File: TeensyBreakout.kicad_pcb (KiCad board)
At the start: 2 copper layers, 149 parts, among them CON1 SJ-3523-SMT-TR, CON2 Headphone, CON3 Line In, IC1 ZLDO1117G33, IC2 NCP1117ST50T3G, J1 73725-0110BLF, J2 Conn_01x02, J3 RJ45_LED, J4 PJ-102A, J5 SPKLEFT, J6 SPKRIGHT, J7 PJ-102A, J8 Conn_01x14, Q1 FDN340P, Q1A1 BSD223P, Q1B1 BSD223P, Q2 BSS138, Q3 AOD417, Q4 BSS138, Q5 BSS138, SW1 SW_MEC_5E, U1 Teensy4.1, U2 ESP-WROOM-02, U3 MAX9744ETH_T, U4 MIC5225-3.3, U5 SGTL5000XNAA3, X1 332-06, X2 Conn_01x05, X3 Conn_01x03

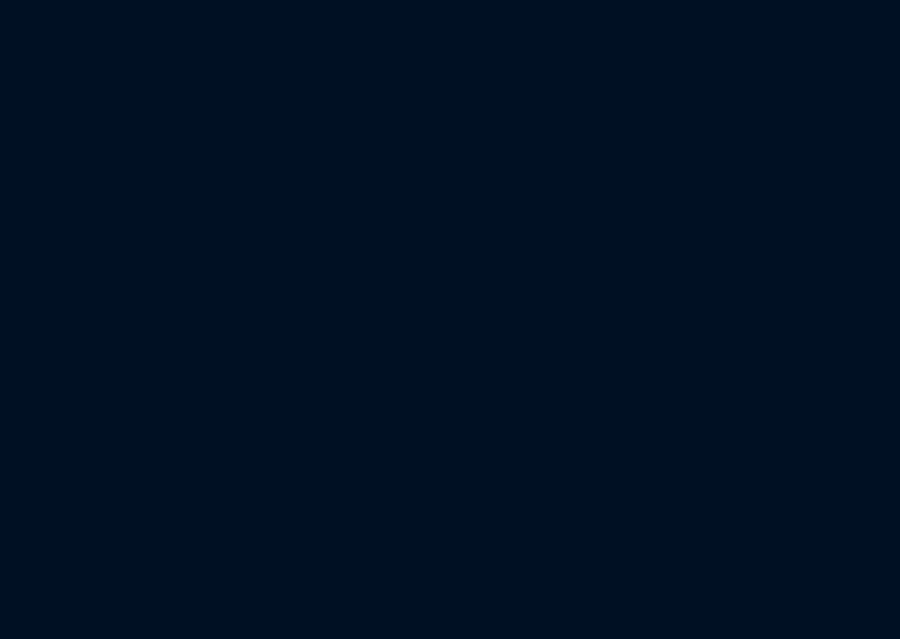
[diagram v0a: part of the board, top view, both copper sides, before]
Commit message: removing old amp, can't buy chip
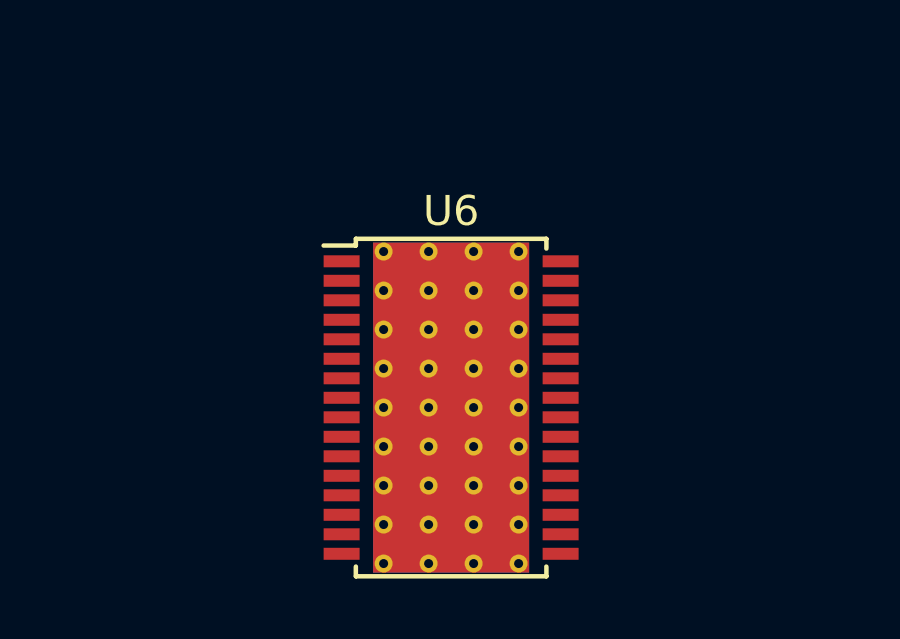
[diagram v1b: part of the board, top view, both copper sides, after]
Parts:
- added U6: TPA3126D2, Package_SO:HTSSOP-32-1EP_6.1x11mm_P0.65mm_EP5.2x11mm_Mask4.11x4.36mm_ThermalVias, F.Cu at (81.6, 121.4)

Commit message: making layout
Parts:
- removed C10, C11, C16, C17: 470pF, Capacitor_SMD:C_0603_1608Metric_Pad1.08x0.95mm_HandSolder
- removed C12, C14: 0.47uF, Capacitor_SMD:C_0603_1608Metric_Pad1.08x0.95mm_HandSolder
- removed C13, C15, C18, C20, C8: 0.1uF, Capacitor_SMD:C_0603_1608Metric_Pad1.08x0.95mm_HandSolder
- removed C19: 2.2uF, Capacitor_SMD:C_0603_1608Metric_Pad1.08x0.95mm_HandSolder
- removed C21: 330uf, Capacitor_THT:CP_Radial_D8.0mm_P3.50mm
- removed C22, C23, C24: 10uF, Capacitor_SMD:C_0603_1608Metric_Pad1.08x0.95mm_HandSolder
- removed CON1: SJ-3523-SMT-TR, digikey-footprints:Switch_Slide_11.6x4mm_SJ-3523-SMT
- removed D2, D3, D4, D5: 1N4148, Diode_SMD:D_0603_1608Metric_Pad1.05x0.95mm_HandSolder
- removed FB1, FB2, FB4, FB5, FB6: MPZ2012S221A, digikey-footprints:0805
- removed J7: PJ-102A, digikey-footprints:Barrel_Jack_5.5mmODx2.1mmID_PJ-102A
- removed J8: Conn_01x14, Connector_PinSocket_2.54mm:PinSocket_1x14_P2.54mm_Vertical
- removed JP14, JP15, JP16, JP17, JP18, JP19, JP20, JP21: SolderJumper_2_Bridged, Jumper:SolderJumper-2_P1.3mm_Bridged_RoundedPad1.0x1.5mm
- removed JP2, JP3, JP4, JP7: SolderJumper_2_Open, Jumper:SolderJumper-2_P1.3mm_Open_TrianglePad1.0x1.5mm
- removed Q2, Q4, Q5: BSS138, digikey-footprints:SOT-23-3
- removed Q3: AOD417, digikey-footprints:TO-252-3
- removed R10, R11, R8, R9: 20K, Resistor_SMD:R_0603_1608Metric_Pad0.98x0.95mm_HandSolder
- removed R12, R13, R14, R15, R16, R17, R18, R5, R6, R7: 10K, Resistor_SMD:R_0603_1608Metric_Pad0.98x0.95mm_HandSolder
- removed RV1: R_POT_Small, Potentiometer_THT:Potentiometer_Bourns_PTV09A-1_Single_Vertical
- removed U3: MAX9744ETH_T, digikey-footprints:TQFN-44-1EP_7x7mm
- removed U4: MIC5225-3.3, Package_TO_SOT_SMD:SOT-23-5_HandSoldering
- removed X1: 332-06, Connector_PinHeader_2.54mm:PinHeader_2x03_P2.54mm_Vertical
- removed X2: Conn_01x05, Connector_PinHeader_2.54mm:PinHeader_1x05_P2.54mm_Vertical
- removed X3: Conn_01x03, digikey-footprints:Term_Block_1x3_P5mm
- added C37: CP_Small, Capacitor_SMD:C_0603_1608Metric_Pad1.08x0.95mm_HandSolder, F.Cu at (51.6, 83.2)
- added C38: CP_Small, Capacitor_SMD:C_0603_1608Metric_Pad1.08x0.95mm_HandSolder, F.Cu at (49.5, 63.5)
- added C39: CP_Small, Capacitor_SMD:C_0603_1608Metric_Pad1.08x0.95mm_HandSolder, F.Cu at (49.5, 61.0)
- added C40: C_Small, Capacitor_SMD:C_0603_1608Metric_Pad1.08x0.95mm_HandSolder, F.Cu at (49.5, 58.4)
- added C41: CP_Small, Capacitor_SMD:C_0603_1608Metric_Pad1.08x0.95mm_HandSolder, F.Cu at (32.6, 78.7)
- added C42: CP_Small, Capacitor_SMD:C_0603_1608Metric_Pad1.08x0.95mm_HandSolder, F.Cu at (31.3, 52.7)
- added C43: C_Small, Capacitor_SMD:C_0603_1608Metric_Pad1.08x0.95mm_HandSolder, F.Cu at (31.3, 54.6)
- added C44: C_Small, Capacitor_SMD:C_0603_1608Metric_Pad1.08x0.95mm_HandSolder, F.Cu at (32.6, 76.8)
- added C45: C_Small, Capacitor_SMD:C_0603_1608Metric_Pad1.08x0.95mm_HandSolder, F.Cu at (32.6, 65.4)
- added Q6: BC107, Package_TO_SOT_THT:TO-18-3, F.Cu at (41.9, 87.0)
- added R23: R_Small, Resistor_SMD:R_0603_1608Metric_Pad0.98x0.95mm_HandSolder, F.Cu at (51.5, 88.9)
- added R24: R_Small, Resistor_SMD:R_0603_1608Metric_Pad0.98x0.95mm_HandSolder, F.Cu at (51.5, 81.3)
- added R25: R_Small, Resistor_SMD:R_0603_1608Metric_Pad0.98x0.95mm_HandSolder, F.Cu at (51.5, 85.1)
- added R26: R_Small, Resistor_SMD:R_0603_1608Metric_Pad0.98x0.95mm_HandSolder, F.Cu at (51.5, 87.0)
- added R27, R31: R_Small, Resistor_SMD:R_0603_1608Metric_Pad0.98x0.95mm_HandSolder, F.Cu at (32.7, 74.9)
- added R28: R_Small, Resistor_SMD:R_0603_1608Metric_Pad0.98x0.95mm_HandSolder, F.Cu at (32.7, 73.0)
- added R29: R_Small, Resistor_SMD:R_0603_1608Metric_Pad0.98x0.95mm_HandSolder, F.Cu at (32.7, 69.2)
- added R30: R_Small, Resistor_SMD:R_0603_1608Metric_Pad0.98x0.95mm_HandSolder, F.Cu at (32.7, 71.1)
- added R32: R_Small, Resistor_SMD:R_0603_1608Metric_Pad0.98x0.95mm_HandSolder, F.Cu at (32.7, 67.3)
- added S1: EG1218, digikey-footprints:Switch_Slide_11.6x4mm_EG1218, F.Cu at (59.8, 58.4)
- added S2: EG1218, digikey-footprints:Switch_Slide_11.6x4mm_EG1218, F.Cu at (59.8, 63.5)
- added Z1: 1N5231BTR, digikey-footprints:DO-35, F.Cu at (47.0, 88.6)
- C1: footprint Capacitor_SMD:C_0603_1608Metric_Pad1.08x0.95mm_HandSolder -> Capacitor_THT:CP_Radial_D5.0mm_P2.50mm
- C6: value 0.1uF -> 10uF
- J2: value Conn_01x02 -> Conn_01x04; footprint TerminalBlock:TerminalBlock_Altech_AK300-2_P5.00mm -> Connector_JST:JST_PH_S4B-PH-K_1x04_P2.00mm_Horizontal
- J5: value SPKLEFT -> OSTTC022162
- J6: value SPKRIGHT -> OSTTC022162
- JP22, SJ1, SJ4, SJ5: moved to B.Cu
- JP8: footprint Connector_PinSocket_2.54mm:PinSocket_2x18_P2.54mm_Vertical -> Connector_PinSocket_2.54mm:PinSocket_2x18_P2.54mm_VerticalFlipped
- L1: footprint digikey-footprints:0603 -> Resistor_SMD:R_0603_1608Metric_Pad0.98x0.95mm_HandSolder
- U6: value TPA3126D2 -> TDA7265; footprint Package_SO:HTSSOP-32-1EP_6.1x11mm_P0.65mm_EP5.2x11mm_Mask4.11x4.36mm_ThermalVias -> Package_TO_SOT_THT:TO-220-11_P3.4x5.08mm_StaggerOdd_Lead4.85mm_Vertical
- VIN1: footprint digikey-footprints:PinHeader_1x2_P2.54mm -> Connector_JST:JST_PH_S2B-PH-K_1x02_P2.00mm_Horizontal
- moved FB3 210.3 mm to (242.1, 60.5)
- moved C34 206.0 mm to (246.7, 60.3)
- moved J3 205.9 mm to (22.0, 74.2), turned to 90 degrees
- moved J1 190.7 mm to (25.4, 84.6), turned to 270 degrees
- moved C3 190.1 mm to (44.5, 111.8), turned to 90 degrees
- moved SJ5 179.5 mm to (52.7, 83.8), turned to 0 degrees
- moved SJ1 178.5 mm to (52.7, 81.3), turned to 0 degrees
- moved JP11 171.8 mm to (55.9, 116.8), turned to 90 degrees
- moved IC2 170.7 mm to (50.8, 111.8), turned to 270 degrees
- moved C2 170.4 mm to (57.1, 111.8), turned to 90 degrees
- moved F1 157.5 mm to (51.2, 116.8)
- moved Q1 151.2 mm to (35.6, 83.8), turned to 180 degrees
- moved JP9 130.4 mm to (78.7, 116.8), turned to 90 degrees
- moved U1 127.3 mm to (44.5, 99.1), turned to 0 degrees
- moved VIN1 122.4 mm to (31.8, 116.8), turned to 0 degrees
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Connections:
- C5 pad 1: /5V_FUSE -> GND
- C5 pad 2: GND -> /5V_FUSE
- C6 pad 1: Net-(C6-Pad1) -> +3V3
- C6 pad 2: Net-(C6-Pad2) -> GND
- J2 pad 1: GND -> Net-(J2-Pad1)
- J2 pad 2: /Amplifier/PWR -> GND
- J5 pad 1: Net-(C16-Pad2) -> Net-(J2-Pad4)
- J5 pad 2: Net-(C17-Pad1) -> GND
- J6 pad 1: Net-(C11-Pad1) -> Net-(J2-Pad1)
- J6 pad 2: Net-(C10-Pad2) -> GND
- JP8 pad 26: /3V3 -> +3V3
- JP8 pad 36: Net-(JP8-Pad36) -> GND
- U1 pad 55: Net-(JP14-Pad2) -> /USB+5V
- U1 pad 56: Net-(JP15-Pad2) -> /D-
- U1 pad 57: Net-(JP16-Pad2) -> /D+
- U1 pad 60: Net-(JP21-Pad1) -> /RX+
- U1 pad 61: Net-(JP20-Pad1) -> /LED
- U1 pad 62: Net-(JP19-Pad1) -> /TX-
- U1 pad 63: Net-(JP18-Pad1) -> /TX+
- U1 pad 65: Net-(JP17-Pad1) -> /RX-
- U6 pad 1: Net-(U6-Pad1) -> Net-(C40-Pad1)
- U6 pad 2: Net-(U6-Pad2) -> Net-(J2-Pad4)
- U6 pad 3: Net-(U6-Pad3) -> VS
- U6 pad 4: Net-(U6-Pad4) -> Net-(J2-Pad1)
- U6 pad 6: Net-(U6-Pad6) -> Net-(C40-Pad1)
- U6 pad 9: Net-(U6-Pad9) -> GND
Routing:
- net /VIN: track 0.00 -> 14.3 mm
- net +5V: track 0.00 -> 9.47 mm
- net /VIN+: track 0.00 -> 8.89 mm
- net /SW-GND: track 0.00 -> 7.99 mm
- net GND: track 0.00 -> 6.65 mm, vias 0 -> 2
- net Net-(D1-PadA): track 0.00 -> 3.86 mm
- added copper zone on F.Cu, net +3V3
- added copper zone on B.Cu, net GND
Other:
- board outline added: 114 x 59 mm

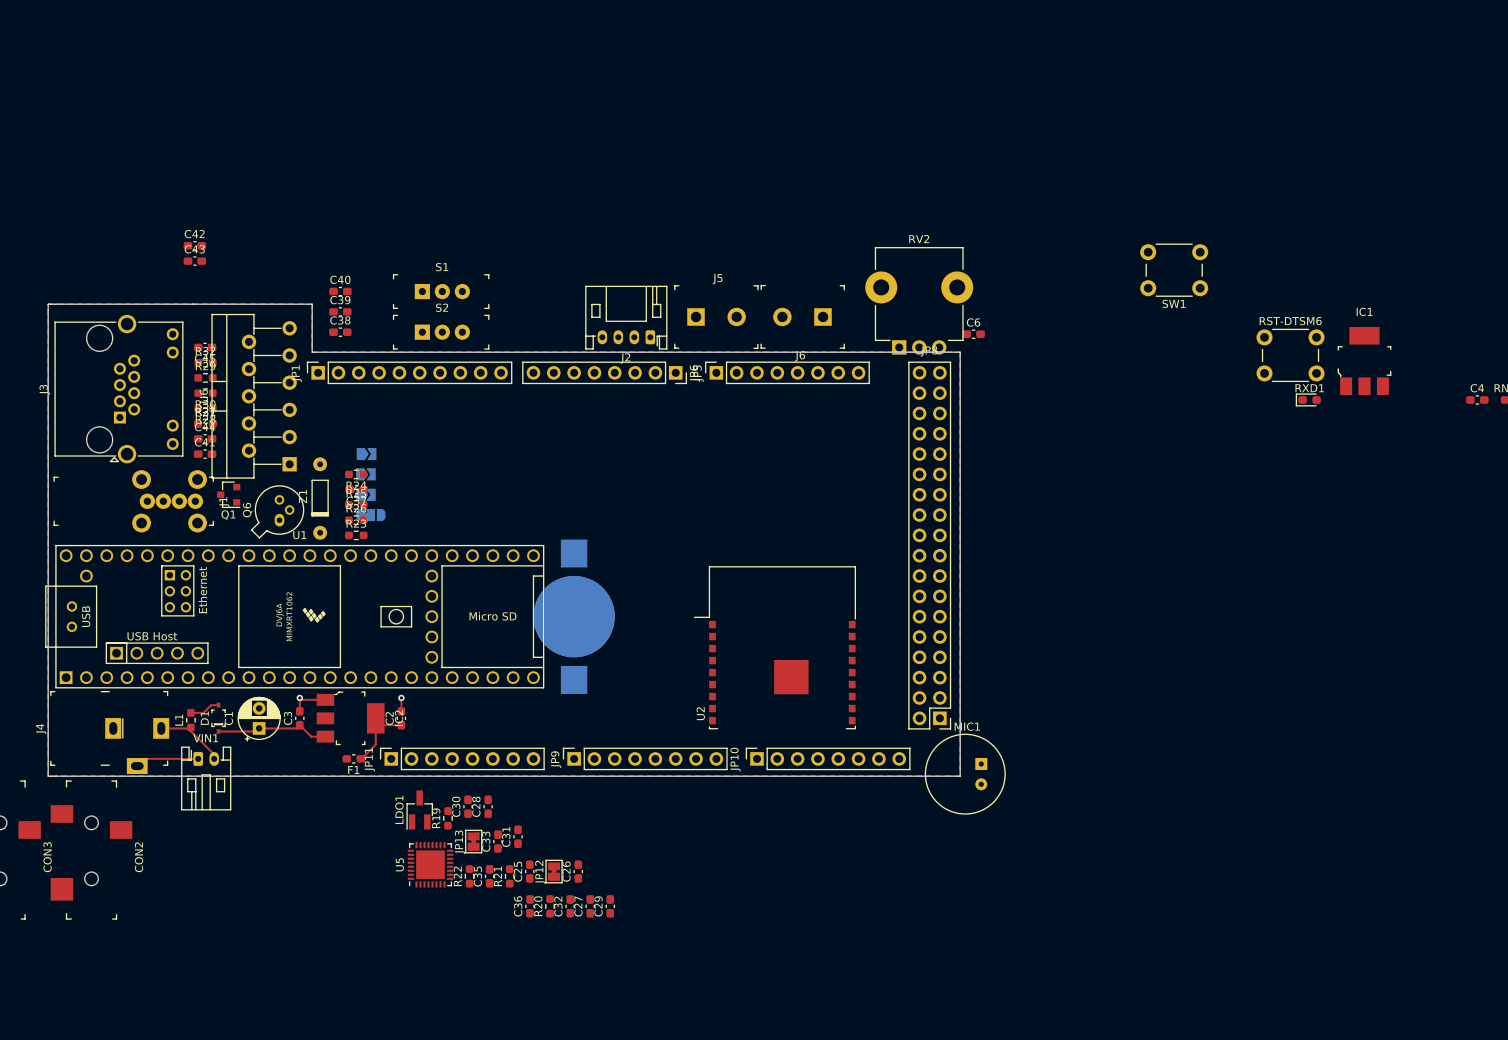
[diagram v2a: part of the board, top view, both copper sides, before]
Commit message: added speaker cutouts
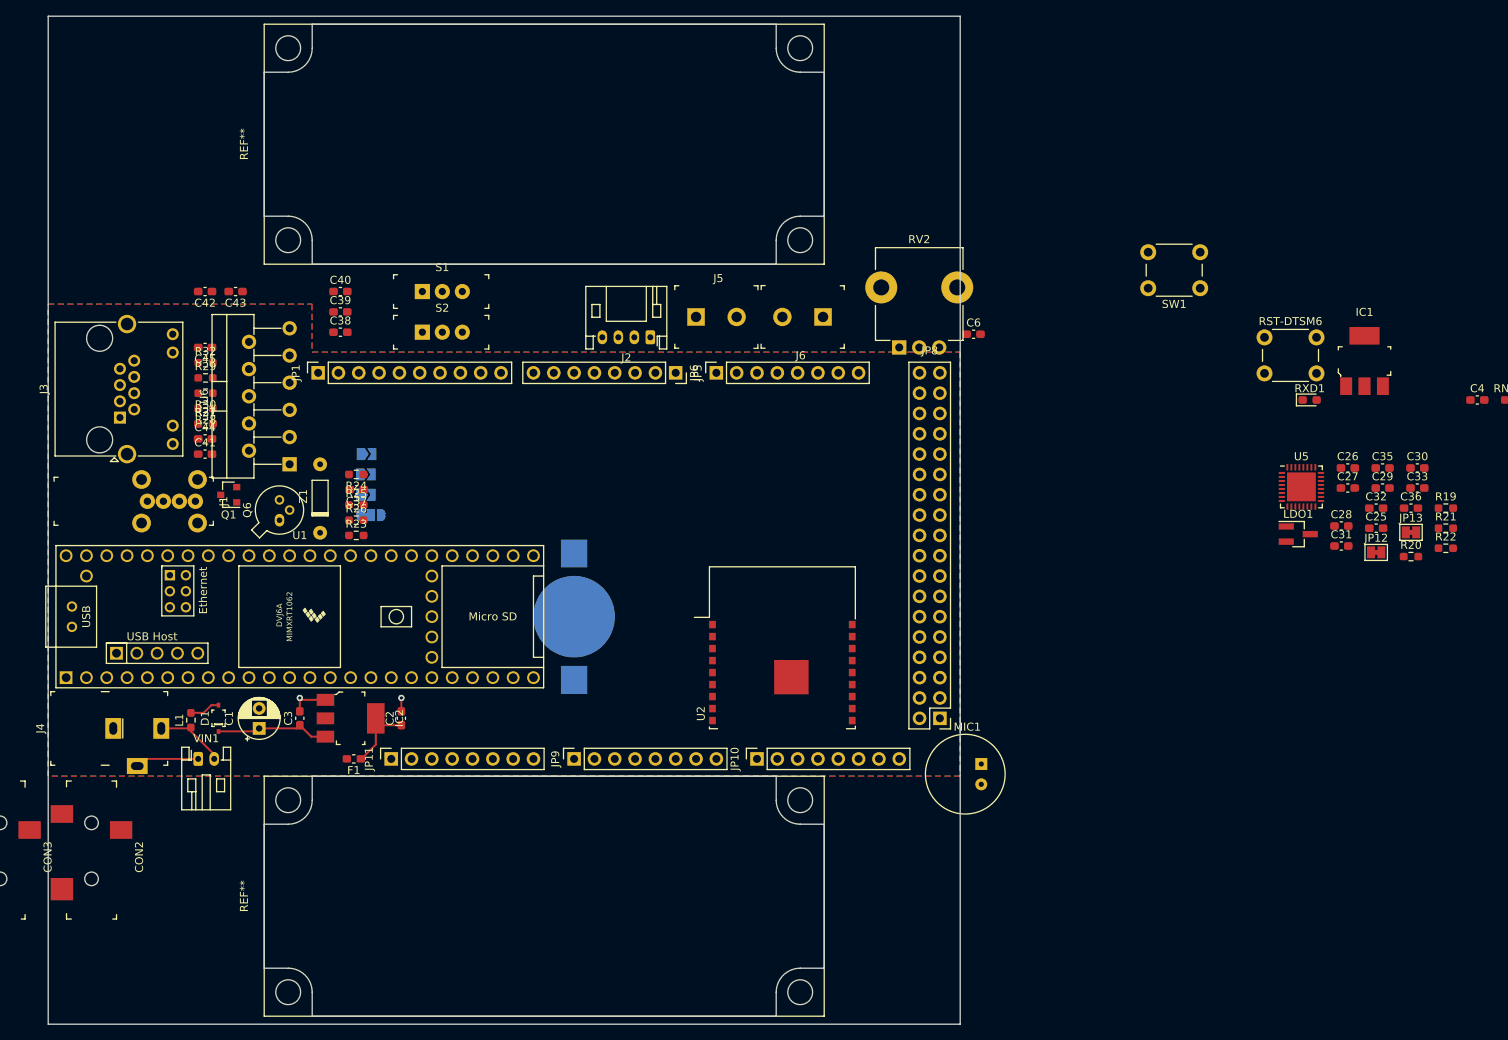
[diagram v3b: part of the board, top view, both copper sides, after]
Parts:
- added REF**: AIYIMA 3070 Speaker, CustomFootprints:AIYIMA 3070 Speaker, F.Cu at (37.0, 40.0)
- added REF**: AIYIMA 3070 Speaker, CustomFootprints:AIYIMA 3070 Speaker, F.Cu at (37.0, 134.0)
- moved R19 130.6 mm to (187.7, 85.5), turned to 0 degrees
- moved R22 128.7 mm to (187.7, 90.5), turned to 0 degrees
- moved C30 126.0 mm to (184.2, 80.5), turned to 0 degrees
- moved R21 124.8 mm to (187.7, 88.0), turned to 0 degrees
- moved JP13 123.4 mm to (183.3, 88.5), turned to 0 degrees
- moved C33 123.1 mm to (184.2, 83.0), turned to 0 degrees
- moved C35 122.7 mm to (179.8, 80.5), turned to 0 degrees
- moved C36 120.9 mm to (183.3, 85.5), turned to 0 degrees
- moved U5 118.7 mm to (169.7, 82.8), turned to 0 degrees
- moved R20 116.2 mm to (183.3, 91.5), turned to 0 degrees
- moved LDO1 115.1 mm to (169.2, 88.7), turned to 0 degrees
- moved C25 114.2 mm to (179.0, 88.0), turned to 0 degrees
- moved C32 112.4 mm to (179.0, 85.5), turned to 0 degrees
- moved C28 112.3 mm to (174.7, 87.7), turned to 0 degrees
- moved JP12 110.2 mm to (179.0, 91.0), turned to 0 degrees
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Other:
- board size 114 x 59 mm -> 114 x 126 mm

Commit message: before downsizing
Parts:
- removed the REF** at (37.0, 40.0)
- removed the REF** at (37.0, 134.0)
- added REF**: AIYIMA 3070 Speaker, CustomFootprints:AIYIMA 3070 Speaker, F.Cu at (42.0, 51.0)
- added REF**: AIYIMA 3070 Speaker, CustomFootprints:AIYIMA 3070 Speaker, F.Cu at (42.0, 134.0)
- J5: value OSTTC022162 -> OSTTC022162 (R)
- J6: value OSTTC022162 -> OSTTC022162 (L)
- moved C34 216.8 mm to (30.0, 52.0), turned to 90 degrees
- moved RN8B1 194.6 mm to (35.3, 129.0), turned to 90 degrees
- moved RN2B1 191.6 mm to (37.3, 136.0), turned to 90 degrees
- moved FB3 180.6 mm to (62.0, 75.0), turned to 180 degrees
- moved RN2A1 179.4 mm to (40.3, 136.0), turned to 90 degrees
- moved C9 175.5 mm to (32.6, 63.5), turned to 180 degrees
- moved Q1B1 175.0 mm to (39.3, 129.0)
- moved Q1A1 174.4 mm to (39.3, 123.0)
- moved RN8A1 168.6 mm to (35.3, 123.0), turned to 270 degrees
- moved C5 153.9 mm to (58.0, 114.3), turned to 180 degrees
- moved SPI1 140.4 mm to (107.2, 111.1), turned to 270 degrees
- moved R4 130.5 mm to (119.9, 124.5)
- moved RN5A1 129.6 mm to (91.0, 89.0)
- moved R3 127.0 mm to (119.9, 127.0), turned to 180 degrees
- moved C4 125.7 mm to (72.4, 111.8), turned to 270 degrees
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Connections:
- net Net-(C38-Pad2) renamed /AmpV2/LEFTIN
- net Net-(C39-Pad2) renamed /AmpV2/RIGHTIN
- net VS renamed /AmpV2/VIN
- J5 pad 1: Net-(J2-Pad4) -> GND
- J5 pad 2: GND -> Net-(J2-Pad4)
- J6 pad 1: Net-(J2-Pad1) -> GND
- J6 pad 2: GND -> Net-(J2-Pad1)
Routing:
- net GND: track 6.65 -> 22.8 mm, vias 2 -> 13
- net /VIN+: track 8.89 -> 19.8 mm
- net +5V: track 9.47 -> 0.00 mm
- net Net-(R29-Pad2): track 0.00 -> 8.79 mm
- net Net-(R27-Pad2): track 0.00 -> 7.30 mm
- net /TeensyAudioShield/D15-A1-RX3-SPDIF_IN: track 0.00 -> 4.26 mm
- net GNDA: track 0.00 -> 4.06 mm
- net /RX1-Q1B-GATE: track 0.00 -> 3.02 mm
- net /SW-GND: track 7.99 -> 6.40 mm
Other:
- board size 114 x 126 mm -> 114 x 115.1 mm

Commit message: gonna try auto-route
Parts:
- removed PRG-DTSM6: ESP-PRG, Button_Switch_THT:SW_PUSH_6mm
- removed U2: ESP-WROOM-02, RF_Module:ESP-WROOM-02
- added MOD1: 2491, digikey-footprints:WIFI_Module_ESP8266_2491, F.Cu at (108.6, 90.8)
- added PRG-DTSM1: ESP-PRG, Button_Switch_THT:SW_PUSH_6mm, F.Cu at (117.5, 52.1)
- added XA**: Arduino_Due_Shield, CustomFootprints:Arduino_Due_Shield, F.Cu at (27.9, 119.4)
- JP12, JP13: moved to B.Cu
- S1, S2: footprint digikey-footprints:Switch_Slide_11.6x4mm_EG1218 -> digikey-footprints:Switch_Slide_JS202011SCQN
- SPI1: footprint Connector_PinSocket_2.54mm:PinSocket_2x03_P2.54mm_Vertical -> CustomFootprints:PinSocket_2x03_P2.54mm_Vertical(Flipped)
- moved SJ4 106.0 mm to (158.0, 66.0), turned to 270 degrees
- moved SJ1 86.2 mm to (123.2, 130.9)
- moved Q1A1 85.8 mm to (124.2, 135.1), turned to 90 degrees
- moved C26 82.1 mm to (124.9, 138.4)
- moved RN8B1 81.8 mm to (116.8, 134.3)
- moved RN8A1 81.6 mm to (116.8, 122.9), turned to 90 degrees
- moved Q1B1 81.0 mm to (120.0, 135.1), turned to 90 degrees
- moved SJ5 80.5 mm to (119.5, 128.7), turned to 90 degrees
- moved RN2B1 79.8 mm to (116.8, 130.5), turned to 270 degrees
- moved C42 78.3 mm to (30.4, 136.7)
- moved RN2A1 77.2 mm to (116.8, 126.6)
- moved C43 76.2 mm to (30.4, 134.4)
- moved C27 75.5 mm to (117.2, 138.4)
- moved JP13 72.6 mm to (150.9, 61.6), turned to 270 degrees
- moved S1 68.1 mm to (61.8, 110.8)
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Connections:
- C34 pad 1: /TeensyAudioShield/D15-A1-RX3-SPDIF_IN -> /D15-A1-RX3-SPDIF_IN
- C34 pad 2: GNDA -> GND
- C37 pad 1: /AmpV2/VIN -> /VIN
- C38 pad 2: /AmpV2/LEFTIN -> /AmpV2/LINEIN_L
- C39 pad 2: /AmpV2/RIGHTIN -> /AmpV2/LINEIN_R
- C42 pad 1: /AmpV2/VIN -> /VIN
- C43 pad 1: /AmpV2/VIN -> /VIN
- JP12 pad 1: /TeensyAudioShield/D7-RX2-OUT1A -> /D7-RX2-OUT1A
- JP13 pad 1: /TeensyAudioShield/D8-TX2-IN1 -> /D8-TX2-IN1
- R19 pad 2: /TeensyAudioShield/D18-A4-SDA0 -> /D18-A4-SDA0
- R20 pad 2: /TeensyAudioShield/D23-A9-CRX1-MCLK1 -> /D23-A9-CRX1-MCLK1
- R21 pad 2: /TeensyAudioShield/D19-A5-SCL0 -> /D19-A5-SCL0
- R24 pad 1: /AmpV2/VIN -> /VIN
- RV2 pad 2: /TeensyAudioShield/D15-A1-RX3-SPDIF_IN -> /D15-A1-RX3-SPDIF_IN
- RV2 pad 3: GNDA -> GND
- S1 pad 1: /AmpV2/VIN -> /VIN
- U5 pad 11: /TeensyAudioShield/RIGHTIN -> /AmpV2/LINEIN_R
- U5 pad 12: /TeensyAudioShield/LEFTIN -> /AmpV2/LINEIN_L
- U5 pad 23: /TeensyAudioShield/D20-A6-TX5-LRCLK1 -> /D20-A6-TX5-LRCLK1
- U5 pad 24: /TeensyAudioShield/D21-A7-RX5-BCLK1 -> /D21-A7-RX5-BCLK1
- U5 pad 27: /TeensyAudioShield/D18-A4-SDA0 -> /D18-A4-SDA0
- U5 pad 29: /TeensyAudioShield/D19-A5-SCL0 -> /D19-A5-SCL0
- U5 pad 7: GNDA -> GND
- U6 pad 3: /AmpV2/VIN -> /VIN
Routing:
- net /VIN: track 14.3 -> 97.0 mm
- net /D28-RX7: track 0.00 -> 50.7 mm
- net /D29-TX7: track 0.00 -> 47.1 mm
- net /D32-OUT1B: track 0.00 -> 45.5 mm
- net /D30-CRX3: track 0.00 -> 45.4 mm
- net /D31-CTX3: track 0.00 -> 45.3 mm
- net Net-(J2-Pad4): track 0.00 -> 44.3 mm, vias 0 -> 1
- net Net-(J2-Pad1): track 0.00 -> 37.4 mm, vias 0 -> 2
- net GND: track 22.8 -> 52.9 mm, vias 13 -> 34
- net Net-(C37-Pad2): track 0.00 -> 28.8 mm
- net Net-(R23-Pad2): track 0.00 -> 27.5 mm
- net Net-(C40-Pad1): track 0.00 -> 19.7 mm, vias 0 -> 1
- net Net-(R25-Pad2): track 0.00 -> 18.4 mm
- net /ESP-RST: track 0.00 -> 12.6 mm
- net Net-(C9-Pad1): track 0.00 -> 12.2 mm
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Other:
- net class Default: clearance 0.2 -> 0.1524; trace_width 0.25 -> 0.1524; via_dia 0.8 -> 0.508; via_drill 0.4 -> 0.254
- rule pad_to_mask_clearance: 0 -> 0.0508
- rule trace_clearance: 0.2 -> 0.1524
- rule trace_min: 0.2 -> 0.1524
- rule via_min_drill: 0.3 -> 0.254
- rule via_min_size: 0.4 -> 0.508
